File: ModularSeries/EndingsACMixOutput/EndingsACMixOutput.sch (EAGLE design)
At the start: 56 parts, among them IC2 LM358

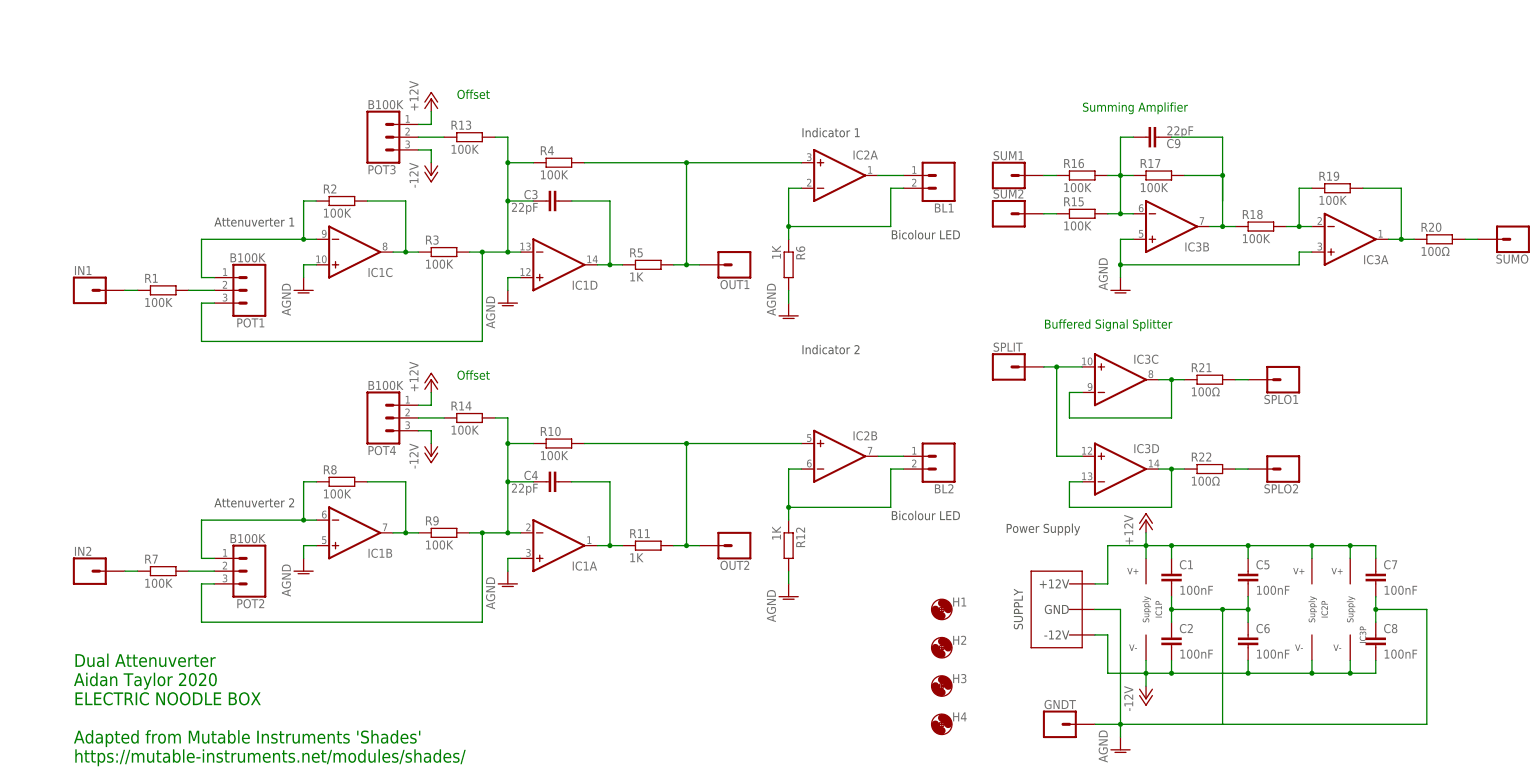
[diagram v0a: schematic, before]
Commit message: TRHP-SVG version 2, Endings added and Mirrors updated
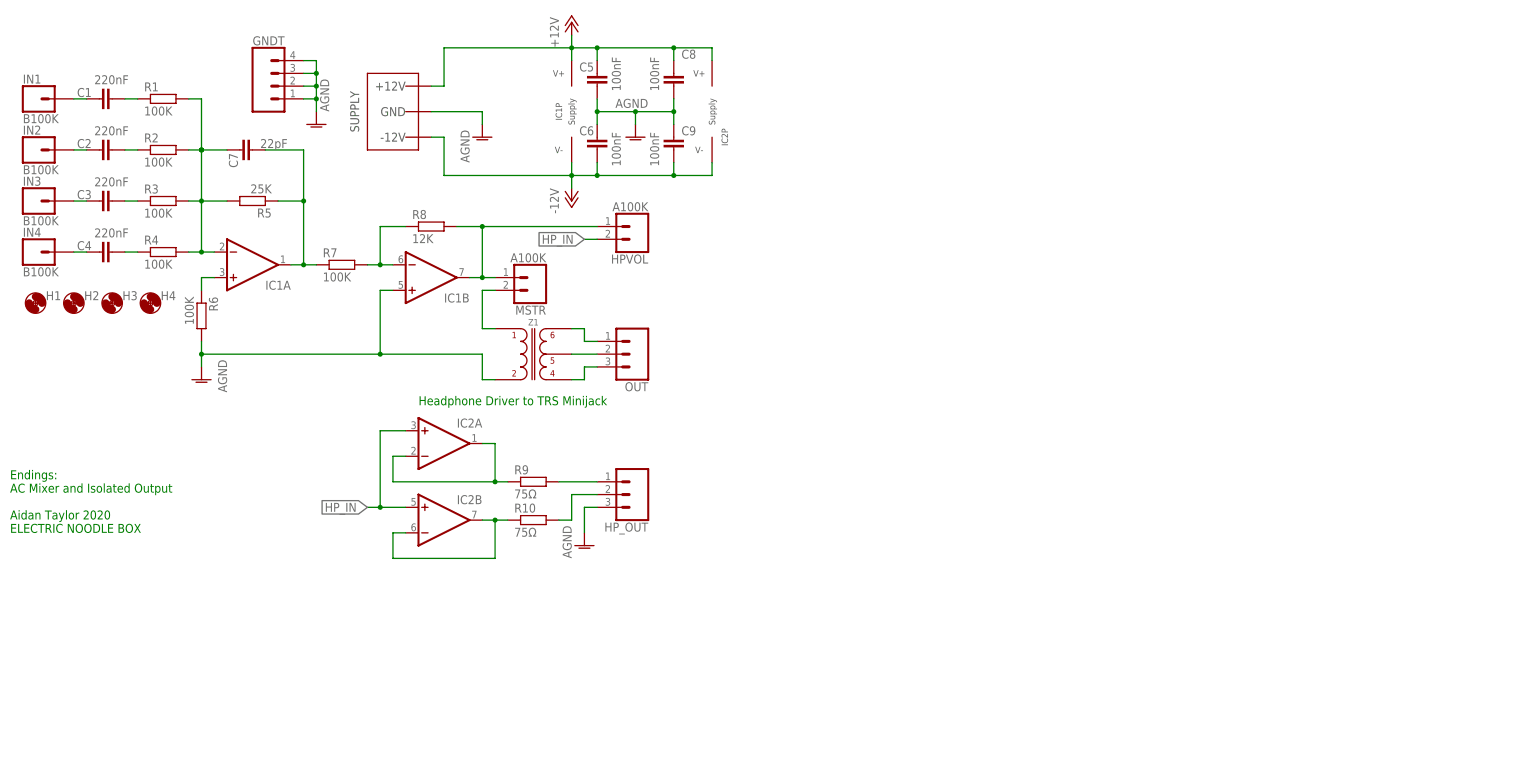
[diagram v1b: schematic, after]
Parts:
- removed BL1, BL2: 2XWIREPAD, ElectricNoodleBox:2XWIREPAD
- removed IC3: (no value), ElectricNoodleBox:TL0X4DIL
- removed OUT1, OUT2, SPLIT, SPLO1, SPLO2, SUM1, SUM2, SUMO: 1XWIREPAD, ElectricNoodleBox:1XWIREPAD
- removed POT1, POT2, POT3, POT4: B100K, ElectricNoodleBox:3XWIREPAD
- removed R11, R12: 1K, rcl:R-EU_0207/10
- removed R13, R14, R15, R16, R17, R18, R19: 100K, rcl:R-EU_0207/10
- removed R20, R21, R22: 100Ω, rcl:R-EU_0207/10
- added HPVOL, MSTR: A100K, ElectricNoodleBox:2XWIREPAD
- added HP_OUT, OUT: 3XWIREPAD, ElectricNoodleBox:3XWIREPAD
- added IN3, IN4: B100K, ElectricNoodleBox:1XWIREPAD
- added Z1: (no value), ElectricNoodleBox:Z1604_AUDIO_TRANSFORMER
- C1, C2: value 100nF -> 220nF
- C3, C4: value 22pF -> 220nF
- C7: value 100nF -> 22pF
- C9: value 22pF -> 100nF
- GNDT: value 1XWIREPAD -> 4XWIREPAD; device ElectricNoodleBox:1XWIREPAD -> ElectricNoodleBox:4XWIREPAD
- IC1: device ElectricNoodleBox:TL0X4DIL -> ElectricNoodleBox:TL0X2DIL
- IC2: value LM358 -> (none); device ElectricNoodleBox:LM358 -> ElectricNoodleBox:TL0X2DIL
- IN1, IN2: value 1XWIREPAD -> B100K
- R10, R9: value 100K -> 75Ω
- R5: value 1K -> 25K
- R6: value 1K -> 100K
- R8: value 100K -> 12K
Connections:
- removed net N$22: POT4.2, R14.1
- removed net N$23: C9.1, IC3B.OUT, R17.2, R18.1
- removed net N$24: IC3A.OUT, R19.2, R20.1
- removed net N$25: R20.2, SUMO.1
- removed net N$26: R16.1, SUM1.1
- removed net N$27: R15.1, SUM2.1
- removed net N$28: IC3C.-IN, IC3C.OUT, R21.1
- removed net N$29: IC3D.-IN, IC3D.OUT, R22.1
- removed net N$30: IC3C.+IN, IC3D.+IN, SPLIT.1
- removed net N$31: R21.2, SPLO1.1
- removed net N$32: R22.2, SPLO2.1
- new net HP_IN: HPVOL.2, IC2A.+IN, IC2B.+IN
- net +12V: now also C8.1; no longer C1.1, C7.1, IC3P.V+, POT3.1, POT4.1
- net -12V: now also C9.2; no longer C2.2, C8.2, IC3P.V-, POT3.3, POT4.3
- net AGND: now also C8.2, C9.1, GNDT.2, GNDT.3, GNDT.4, HP_OUT.3, Z1.3; no longer C1.2, C2.1, C7.2, C8.1, IC1A.+IN, IC1C.+IN, IC1D.+IN, IC3A.+IN, IC3B.+IN, R12.2
- net N$1: now also C4.1, IN4.1; no longer POT1.2, R1.2
- net N$10: now also C3.2, R3.1; no longer IC3A.-IN, R18.2, R19.1
- net N$11: now also C4.2, R4.1; no longer IC1B.-IN, POT2.1, R8.1
- net N$12: now also C2.1, IN2.1; no longer IC1B.OUT, R8.2, R9.1
- net N$13: now also C1.1, IN1.1; no longer C4.1, IC1A.-IN, POT2.3, R10.1, R14.2, R9.2
- net N$14: now also MSTR.2, Z1.1; no longer IC2B.+IN, OUT2.1, R10.2, R11.2
- net N$15: now also OUT.1, Z1.6; no longer C4.2, IC1A.OUT, R11.1
- net N$16: now also OUT.2, Z1.5; no longer IN2.1, R7.1
- net N$17: now also OUT.3, Z1.4; no longer BL2.1, IC2B.OUT
- net N$18: now also IC2A.-IN, IC2A.OUT, R9.1; no longer BL2.2, IC2B.-IN, R12.1
- net N$19: now also HP_OUT.1, R9.2; no longer BL1.2, IC2A.-IN, R6.1
- net N$2: now also C7.1, IC1A.-IN, R1.2, R2.2, R3.2, R4.2, R5.2; no longer IC1C.-IN, POT1.1, R2.1
- net N$20: now also IC2B.-IN, IC2B.OUT, R10.1; no longer POT3.2, R13.1
- net N$21: now also HP_OUT.2, R10.2; no longer C9.2, IC3B.-IN, R15.2, R16.2, R17.1
- net N$3: now also C7.2, IC1A.OUT, R5.1, R7.1; no longer POT2.2, R7.2
- net N$4: now also IC1B.-IN, R7.2, R8.1; no longer IC1C.OUT, R2.2, R3.1
- net N$5: now also HPVOL.1, IC1B.OUT, MSTR.1, R8.2; no longer C3.1, IC1D.-IN, POT1.3, R13.2, R3.2, R4.1
- net N$6: now also C3.1, IN3.1; no longer IC2A.+IN, OUT1.1, R4.2, R5.2
- net N$7: now also IC1A.+IN, R6.1; no longer C3.2, IC1D.OUT, R5.1
- net N$8: now also C1.2, R1.1; no longer BL1.1, IC2A.OUT
- net N$9: now also C2.2, R2.1; no longer IN1.1, R1.1
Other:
- note added: "Endings: AC Mixer and Isolated Output Aidan Taylor 2020 ELECTRIC NOODLE BOX"
- note added: "Headphone Driver to TRS Minijack"
- note removed: "Attenuverter 1"
- note removed: "Attenuverter 2"
- note removed: "Bicolour LED"
- note removed: "Buffered Signal Splitter"
- note removed: "Dual Attenuverter Aidan Taylor 2020 ELECTRIC NOODLE BOX Adapted from Mutable Instruments 'Shades' https://mutable-instruments.net/modules/shades/"
- note removed: "Indicator 1"
- note removed: "Indicator 2"
- note removed: "Offset"
- note removed: "Power Supply"
- note removed: "Summing Amplifier"
- moved on the sheet: C1, C2, C3, C4, C5, C6, C7, C8, C9, H1, H2, H3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

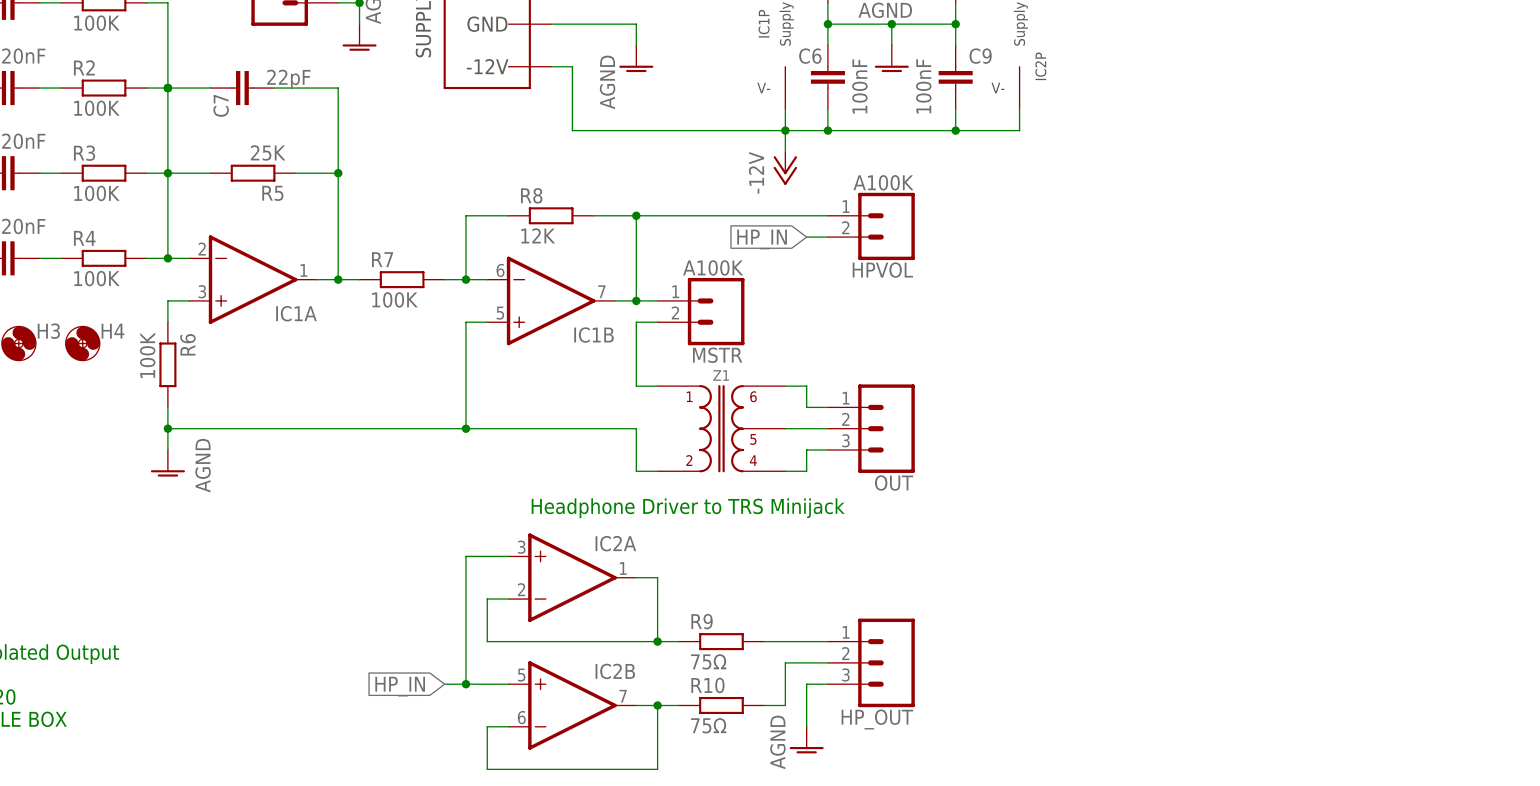
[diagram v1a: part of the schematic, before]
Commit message: Schematic and layout update to Endings
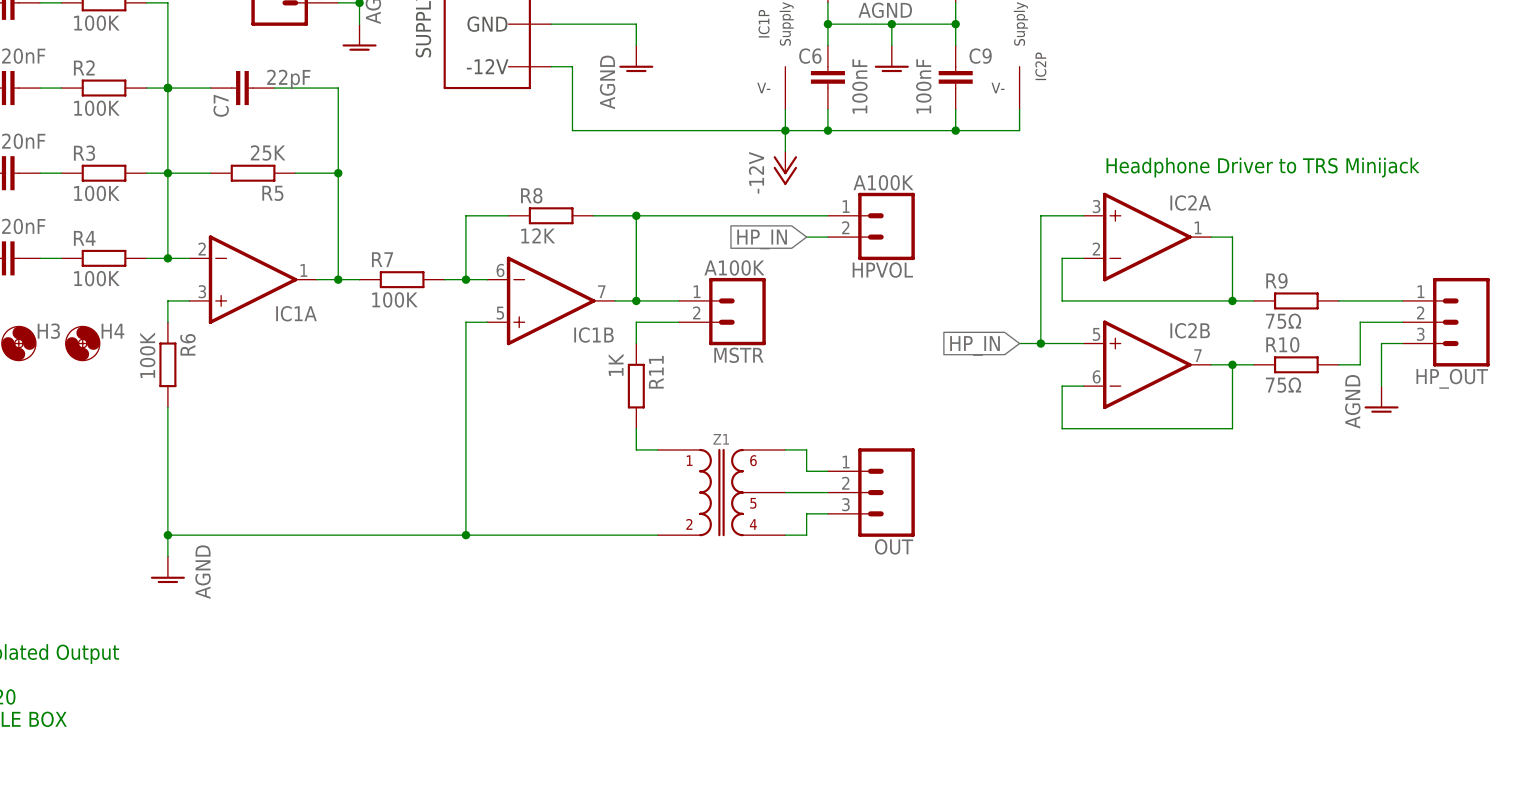
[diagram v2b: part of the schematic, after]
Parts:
- added R11: 1K, rcl:R-EU_0207/10
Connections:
- new net N$22: R11.2, Z1.1
- net N$14: now also R11.1; no longer Z1.1
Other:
- moved on the sheet: HP_OUT, IC2A, IC2B, MSTR, OUT, R10, R9, Z1

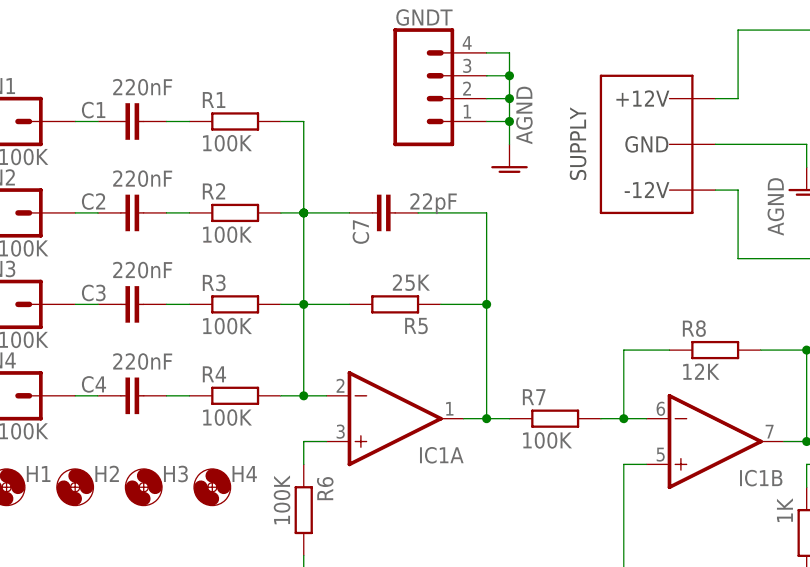
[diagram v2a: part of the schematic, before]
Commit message: Endings BOM added
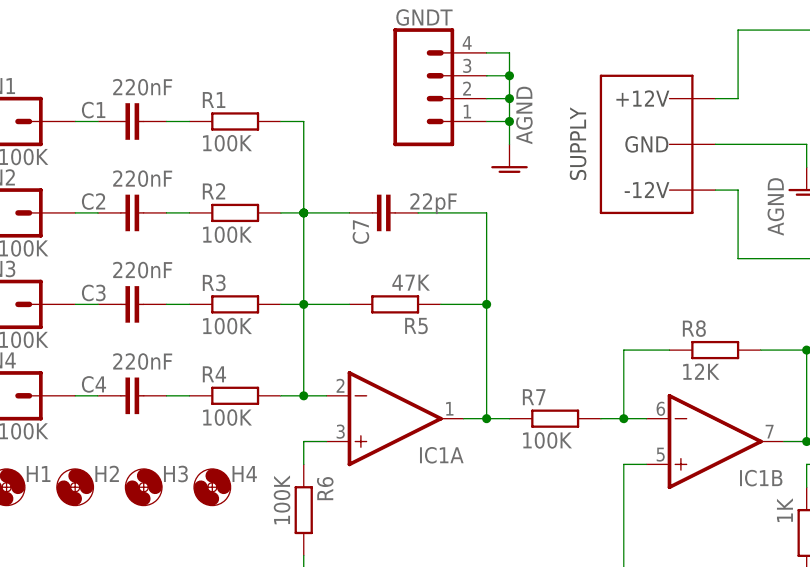
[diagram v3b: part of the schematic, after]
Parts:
- R5: value 25K -> 47K
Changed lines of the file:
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@@
 <part name="R3" library="rcl" library_urn="urn:adsk.eagle:library:334" deviceset="R-EU_" device="0207/10" package3d_urn="urn:adsk.eagle:package:23491/2" value="100K"/>
 <part name="R4" library="rcl" library_urn="urn:adsk.eagle:library:334" deviceset="R-EU_" device="0207/10" package3d_urn="urn:adsk.eagle:package:23491/2" value="100K"/>
-<part name="R5" library="rcl" library_urn="urn:adsk.eagle:library:334" deviceset="R-EU_" device="0207/10" package3d_urn="urn:adsk.eagle:package:23491/2" value="25K"/>
+<part name="R5" library="rcl" library_urn="urn:adsk.eagle:library:334" deviceset="R-EU_" device="0207/10" package3d_urn="urn:adsk.eagle:package:23491/2" value="47K"/>
 <part name="C1" library="rcl" library_urn="urn:adsk.eagle:library:334" deviceset="C-EU" device="050-025X075" package3d_urn="urn:adsk.eagle:package:23637/1" value="220nF"/>
 <part name="C2" library="rcl" library_urn="urn:adsk.eagle:library:334" deviceset="C-EU" device="050-025X075" package3d_urn="urn:adsk.eagle:package:23637/1" value="220nF"/>

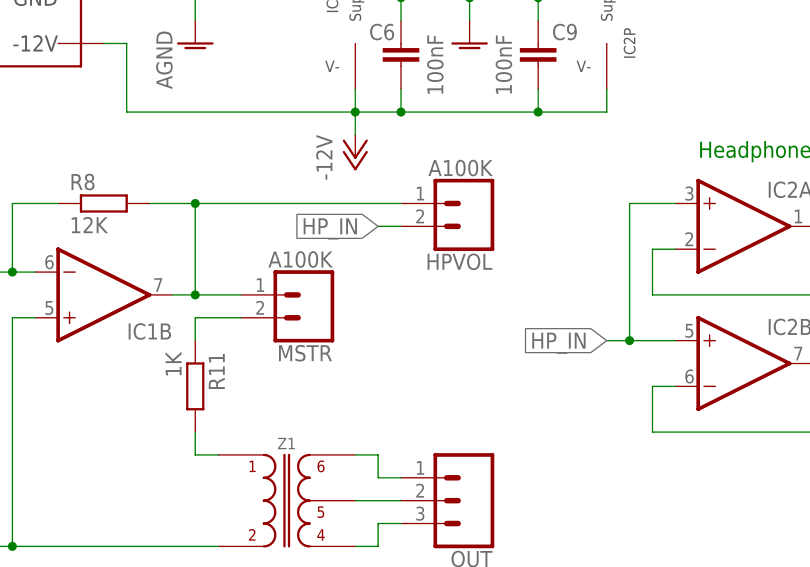
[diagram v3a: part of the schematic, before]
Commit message: Layout and schematic renders for LHP added
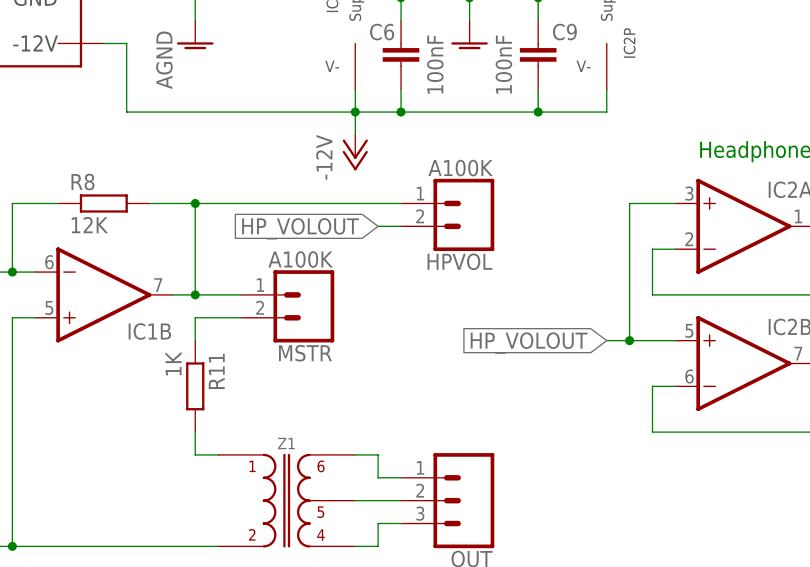
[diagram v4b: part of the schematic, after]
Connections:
- net HP_IN renamed HP_VOLOUT
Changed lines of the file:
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@@
 <?xml version="1.0" encoding="utf-8"?>
 <!DOCTYPE eagle SYSTEM "eagle.dtd">
-<eagle version="9.6.0">
+<eagle version="9.6.2">
 <drawing>
 <settings>
@@
 </segment>
 </net>
-<net name="HP_IN" class="0">
+<net name="HP_VOLOUT" class="0">
 <segment>
 <pinref part="HPVOL" gate="G$1" pin="2"/>
